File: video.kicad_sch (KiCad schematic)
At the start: 4 parts, among them J1 Video Output Female, J2 Board Interconnect Female, J3 Conn_02x08_Odd_Even

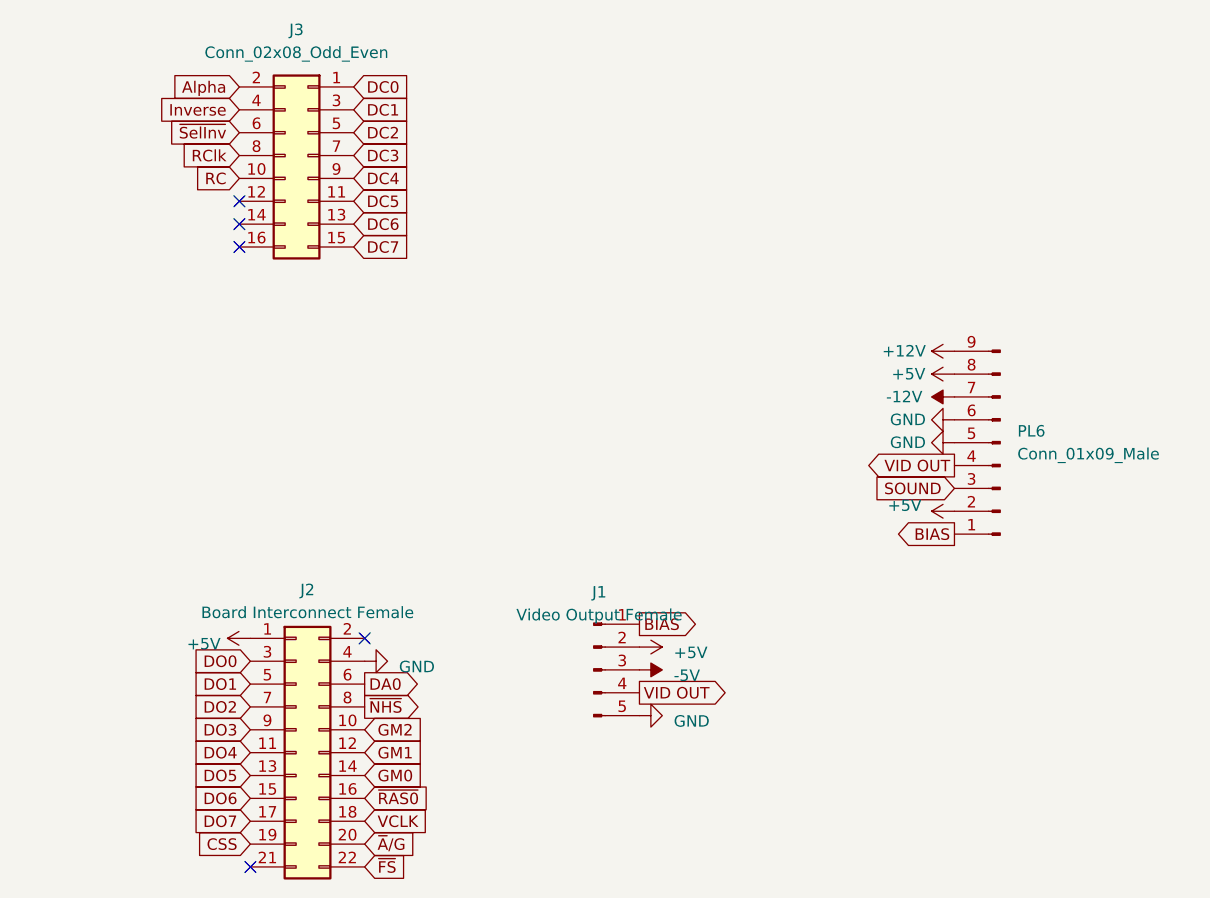
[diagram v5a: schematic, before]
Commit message: switch to fpga
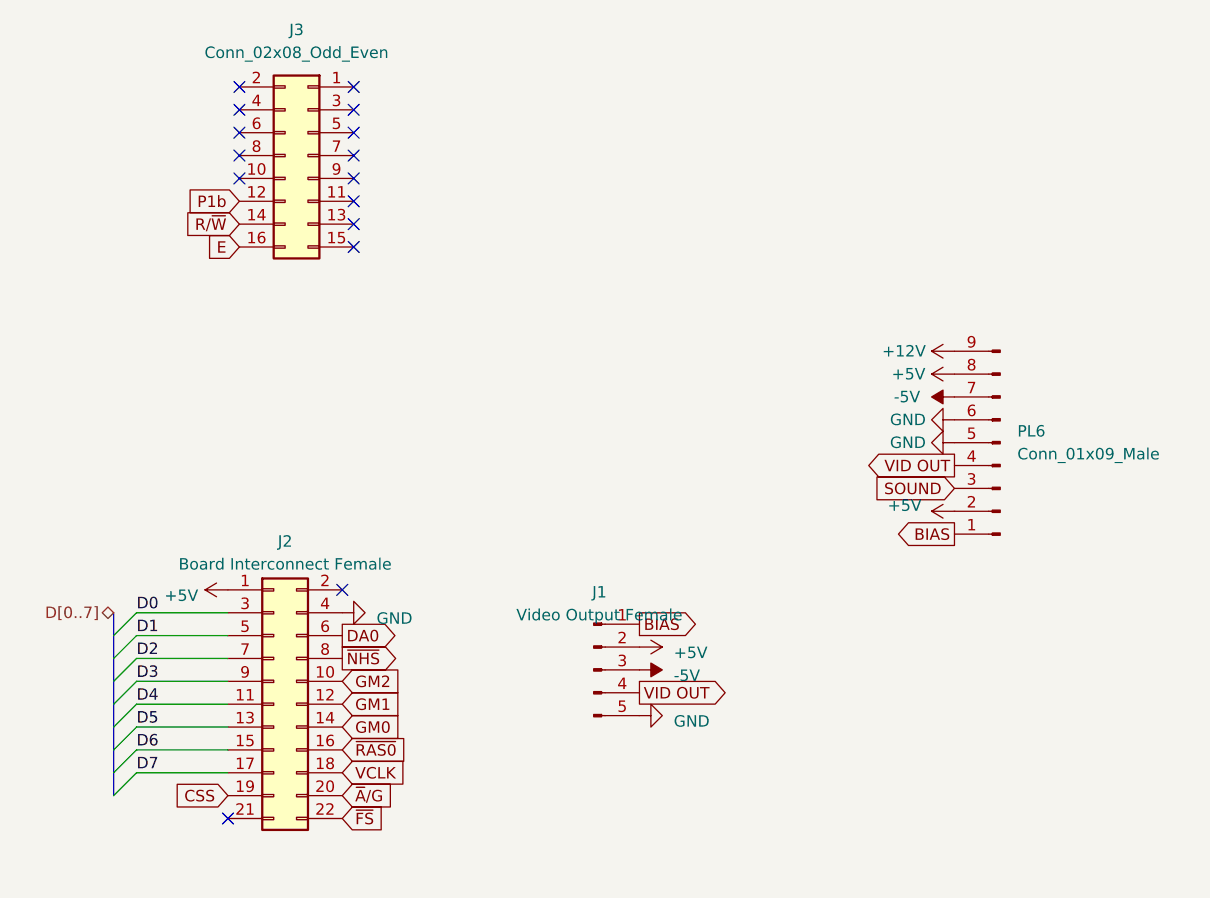
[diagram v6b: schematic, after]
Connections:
- net -12V is gone; now on net -5V: PL6.7 (Pin_7)
- net P1b: now reaches J3.12 (Pin_12)
- net R/~{W}: now reaches J3.14 (Pin_14)
- net E: now reaches J3.16 (Pin_16)
- net Alpha: no longer names the net of J3.2 (Pin_2)
- net DC0: no longer names the net of J3.1 (Pin_1)
- net DC1: no longer names the net of J3.3 (Pin_3)
- net DC2: no longer names the net of J3.5 (Pin_5)
- net DC3: no longer names the net of J3.7 (Pin_7)
- net DC4: no longer names the net of J3.9 (Pin_9)
- net DC5: no longer names the net of J3.11 (Pin_11)
- net DC6: no longer names the net of J3.13 (Pin_13)
- net DC7: no longer names the net of J3.15 (Pin_15)
- net DO0 renamed D0
- net DO1 renamed D1
- net DO2 renamed D2
- net DO3 renamed D3
- net DO4 renamed D4
- net DO5 renamed D5
- net DO6 renamed D6
- net DO7 renamed D7
- net Inverse: no longer names the net of J3.4 (Pin_4)
- net RC: no longer names the net of J3.10 (Pin_10)
- net RClk: no longer names the net of J3.8 (Pin_8)
- net ~{SelInv}: no longer names the net of J3.6 (Pin_6)
- no-connect marks 5 -> 15
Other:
- moved on the sheet: J2
